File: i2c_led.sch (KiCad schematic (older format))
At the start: 20 parts

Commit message: Worked on BOM.
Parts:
- gave numbers to parts that had none: 20
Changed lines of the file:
@@
 $EndDescr
 $Comp
-L ME2188:ME2188A50XG U?
+L ME2188:ME2188A50XG U2
 U 1 1 6174A4C9
 P 2750 1500
-F 0 "U?" H 2750 1915 50  0000 C CNN
+F 0 "U2" H 2750 1915 50  0000 C CNN
 F 1 "ME2188A50XG" H 2750 1824 50  0000 C CNN
 F 2 "" H 2750 2000 50  0001 C CNN
@@
 $EndComp
 $Comp
-L pspice:INDUCTOR L?
+L pspice:INDUCTOR L1
 U 1 1 6174AC13
 P 1950 1400
-F 0 "L?" H 1950 1615 50  0000 C CNN
+F 0 "L1" H 1950 1615 50  0000 C CNN
 F 1 "22uH" H 1950 1524 50  0000 C CNN
 F 2 "" H 1950 1400 50  0001 C CNN
@@
 	2200 1400 2350 1400
 $Comp
-L power:GND #PWR?
+L power:GND #PWR05
 U 1 1 6174B335
 P 2750 2000
-F 0 "#PWR?" H 2750 1750 50  0001 C CNN
+F 0 "#PWR05" H 2750 1750 50  0001 C CNN
 F 1 "GND" H 2755 1827 50  0000 C CNN
 F 2 "" H 2750 2000 50  0001 C CNN
@@
 $EndComp
 $Comp
-L Device:C C?
+L Device:C C1
 U 1 1 6174BB29
 P 1475 1725
-F 0 "C?" H 1590 1771 50  0000 L CNN
+F 0 "C1" H 1590 1771 50  0000 L CNN
 F 1 "10uF" H 1590 1680 50  0000 L CNN
 F 2 "" H 1513 1575 50  0001 C CNN
@@
 	1475 2000 1475 1875
 $Comp
-L power:GND #PWR?
+L power:GND #PWR01
 U 1 1 6174C089
 P 1475 2000
-F 0 "#PWR?" H 1475 1750 50  0001 C CNN
+F 0 "#PWR01" H 1475 1750 50  0001 C CNN
 F 1 "GND" H 1480 1827 50  0000 C CNN
 F 2 "" H 1475 2000 50  0001 C CNN
@@
 VIN
 $Comp
-L Device:C C?
+L Device:C C4
 U 1 1 6174D112
 P 3475 1725
-F 0 "C?" H 3590 1771 50  0000 L CNN
+F 0 "C4" H 3590 1771 50  0000 L CNN
 F 1 "100uF" H 3590 1680 50  0000 L CNN
 F 2 "" H 3513 1575 50  0001 C CNN
@@
 	3475 2000 3475 1875
 $Comp
-L power:GND #PWR?
+L power:GND #PWR06
 U 1 1 6174E073
 P 3475 2000
-F 0 "#PWR?" H 3475 1750 50  0001 C CNN
+F 0 "#PWR06" H 3475 1750 50  0001 C CNN
 F 1 "GND" H 3480 1827 50  0000 C CNN
 F 2 "" H 3475 2000 50  0001 C CNN
@@
 \nDC-DC converter input 1.8-5V, output 5V\nLCSC Part# C236769
 $Comp
-L Connector_Generic:Conn_01x04 J?
+L Connector_Generic:Conn_01x04 J1
 U 1 1 617588B6
 P 8450 1425
-F 0 "J?" H 8530 1417 50  0000 L CNN
+F 0 "J1" H 8530 1417 50  0000 L CNN
 F 1 "Conn_01x04" H 8530 1326 50  0000 L CNN
 F 2 "" H 8450 1425 50  0001 C CNN
@@
 $EndComp
 $Comp
-L Connector_Generic:Conn_01x04 J?
+L Connector_Generic:Conn_01x04 J2
 U 1 1 617591D1
 P 10050 1425
-F 0 "J?" H 10130 1417 50  0000 L CNN
+F 0 "J2" H 10130 1417 50  0000 L CNN
 F 1 "Conn_01x04" H 10130 1326 50  0000 L CNN
 F 2 "" H 10050 1425 50  0001 C CNN
@@
 SCL_VIN
 $Comp
-L Potentiometer_Digital:MCP4018-xxxxLT U?
+L Potentiometer_Digital:MCP4018-xxxxLT U1
 U 1 1 6175D2CA
 P 1850 4575
-F 0 "U?" H 1850 5050 50  0000 C CNN
+F 0 "U1" H 1850 5050 50  0000 C CNN
 F 1 "MCP4018-xxxxLT" H 2125 4950 50  0000 C CNN
 F 2 "Package_TO_SOT_SMD:SOT-363_SC-70-6" H 1900 4325 50  0001 L CNN
@@
 	1850 5000 1850 4875
 $Comp
-L power:GND #PWR?
+L power:GND #PWR02
 U 1 1 6175F273
 P 1850 5000
-F 0 "#PWR?" H 1850 4750 50  0001 C CNN
+F 0 "#PWR02" H 1850 4750 50  0001 C CNN
 F 1 "GND" H 1855 4827 50  0000 C CNN
 F 2 "" H 1850 5000 50  0001 C CNN
@@
 Stemma QT / qwiic  connectors\nLCSC#  C145956
 $Comp
-L Transistor_FET:BSS138 Q?
+L Transistor_FET:BSS138 Q3
 U 1 1 61765AC4
 P 9100 5000
-F 0 "Q?" V 9349 5000 50  0000 C CNN
+F 0 "Q3" V 9349 5000 50  0000 C CNN
 F 1 "BSS138" V 9440 5000 50  0000 C CNN
 F 2 "Package_TO_SOT_SMD:SOT-23" H 9300 4925 50  0001 L CIN
@@
 $EndComp
 $Comp
-L Transistor_FET:BSS138 Q?
+L Transistor_FET:BSS138 Q2
 U 1 1 61767FC9
 P 8600 4400
-F 0 "Q?" V 8849 4400 50  0000 C CNN
+F 0 "Q2" V 8849 4400 50  0000 C CNN
 F 1 "BSS138" V 8940 4400 50  0000 C CNN
 F 2 "Package_TO_SOT_SMD:SOT-23" H 8800 4325 50  0001 L CIN
@@
 i2c level shifters\nBSS138 LCSC# C78284
 $Comp
-L Device:R R?
+L Device:R R4
 U 1 1 61771F4B
 P 8000 4175
-F 0 "R?" H 8070 4221 50  0000 L CNN
+F 0 "R4" H 8070 4221 50  0000 L CNN
 F 1 "10k" H 8070 4130 50  0000 L CNN
 F 2 "" V 7930 4175 50  0001 C CNN
@@
 $EndComp
 $Comp
-L Device:R R?
+L Device:R R3
 U 1 1 61772E16
 P 7675 4175
-F 0 "R?" H 7745 4221 50  0000 L CNN
+F 0 "R3" H 7745 4221 50  0000 L CNN
 F 1 "10k" H 7745 4130 50  0000 L CNN
 F 2 "" V 7605 4175 50  0001 C CNN
@@
 $EndComp
 $Comp
-L Device:R R?
+L Device:R R6
 U 1 1 61773986
 P 9900 4175
-F 0 "R?" H 9970 4221 50  0000 L CNN
+F 0 "R6" H 9970 4221 50  0000 L CNN
 F 1 "10k" H 9970 4130 50  0000 L CNN
 F 2 "" V 9830 4175 50  0001 C CNN
@@
 $EndComp
 $Comp
-L Device:R R?
+L Device:R R5
 U 1 1 61773B5E
 P 9575 4175
-F 0 "R?" H 9645 4221 50  0000 L CNN
+F 0 "R5" H 9645 4221 50  0000 L CNN
 F 1 "10k" H 9645 4130 50  0000 L CNN
 F 2 "" V 9505 4175 50  0001 C CNN
@@
 MCP4018T-503E/LT\nLCSC# C145561
 $Comp
-L Amplifier_Operational:LMV321 U?
+L Amplifier_Operational:LMV321 U3
 U 1 1 617B3880
 P 3675 4575
-F 0 "U?" H 4019 4621 50  0000 L CNN
+F 0 "U3" H 4019 4621 50  0000 L CNN
 F 1 "LMV321" H 4019 4530 50  0000 L CNN
 F 2 "" H 3675 4575 50  0001 L CNN
@@
 $EndComp
 $Comp
-L Device:R R?
+L Device:R R1
 U 1 1 617B515A
 P 2650 4375
-F 0 "R?" V 2443 4375 50  0000 C CNN
+F 0 "R1" V 2443 4375 50  0000 C CNN
 F 1 "45.3k" V 2534 4375 50  0000 C CNN
 F 2 "" V 2580 4375 50  0001 C CNN
@@
 45.3k  1% 0603 resistor C23058\n24.9    1% 0603  resistor C403105
 $Comp
-L Device:LED_ALT D?
+L Device:LED_ALT D1
 U 1 1 617C0FF2
 P 4875 4050
-F 0 "D?" V 4914 3932 50  0000 R CNN
+F 0 "D1" V 4914 3932 50  0000 R CNN
 F 1 "LED_ALT" V 4823 3932 50  0000 R CNN
 F 2 "" H 4875 4050 50  0001 C CNN
@@
 $EndComp
 $Comp
-L Device:Q_NPN_BEC Q?
+L Device:Q_NPN_BEC Q1
 U 1 1 617C2C7F
 P 4775 4575
-F 0 "Q?" H 4966 4621 50  0000 L CNN
+F 0 "Q1" H 4966 4621 50  0000 L CNN
 F 1 "Q_NPN_BEC" H 4966 4530 50  0000 L CNN
 F 2 "" H 4975 4675 50  0001 C CNN
@@
 	3975 4575 4575 4575
 $Comp
-L Device:R R?
+L Device:R R2
 U 1 1 617C7054
 P 4875 5125
-F 0 "R?" H 4945 5171 50  0000 L CNN
+F 0 "R2" H 4945 5171 50  0000 L CNN
 F 1 "24.9" H 4945 5080 50  0000 L CNN
 F 2 "" V 4805 5125 50  0001 C CNN
@@
 $EndComp
 $Comp
-L power:GND #PWR?
+L power:GND #PWR07
 U 1 1 617BDEF2
 P 3575 5000
-F 0 "#PWR?" H 3575 4750 50  0001 C CNN
+F 0 "#PWR07" H 3575 4750 50  0001 C CNN
 F 1 "GND" H 3580 4827 50  0000 C CNN
 F 2 "" H 3575 5000 50  0001 C CNN
@@
 	3575 5000 3575 4875
 $Comp
-L power:GND #PWR?
+L power:GND #PWR08
 U 1 1 617C9AE1
 P 4875 5400
-F 0 "#PWR?" H 4875 5150 50  0001 C CNN
+F 0 "#PWR08" H 4875 5150 50  0001 C CNN
 F 1 "GND" H 4880 5227 50  0000 C CNN
 F 2 "" H 4875 5400 50  0001 C CNN
@@
 Sikor S8050\nC444723
 $Comp
-L Device:C C?
+L Device:C C2
 U 1 1 617EFAB2
 P 1875 5900
-F 0 "C?" H 1990 5946 50  0000 L CNN
+F 0 "C2" H 1990 5946 50  0000 L CNN
 F 1 "0.1uF" H 1990 5855 50  0000 L CNN
 F 2 "" H 1913 5750 50  0001 C CNN
@@
 $EndComp
 $Comp
-L Device:C C?
+L Device:C C3
 U 1 1 617F0FE6
 P 2650 5900
-F 0 "C?" H 2765 5946 50  0000 L CNN
+F 0 "C3" H 2765 5946 50  0000 L CNN
 F 1 "0.1uF" H 2765 5855 50  0000 L CNN
 F 2 "" H 2688 5750 50  0001 C CNN
@@
 	1875 6175 1875 6050
 $Comp
-L power:GND #PWR?
+L power:GND #PWR03
 U 1 1 617FDA2D
 P 1875 6175
-F 0 "#PWR?" H 1875 5925 50  0001 C CNN
+F 0 "#PWR03" H 1875 5925 50  0001 C CNN
 F 1 "GND" H 1880 6002 50  0000 C CNN
 F 2 "" H 1875 6175 50  0001 C CNN
@@
 	2650 6175 2650 6050
 $Comp
-L power:GND #PWR?
+L power:GND #PWR04
 U 1 1 618001D5
 P 2650 6175
-F 0 "#PWR?" H 2650 5925 50  0001 C CNN
+F 0 "#PWR04" H 2650 5925 50  0001 C CNN
 F 1 "GND" H 2655 6002 50  0000 C CNN
 F 2 "" H 2650 6175 50  0001 C CNN

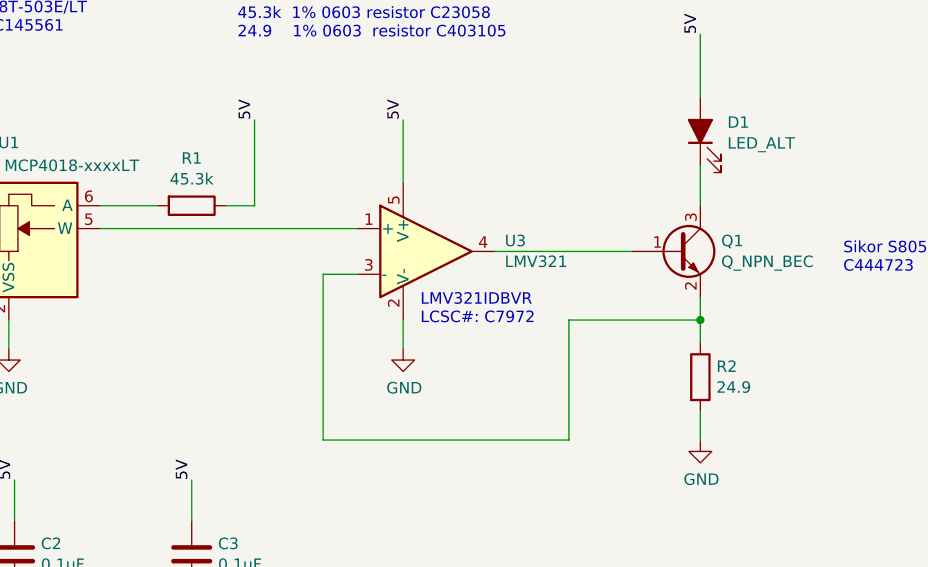
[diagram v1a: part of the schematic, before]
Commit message: Work on BOM and footprint assignments.
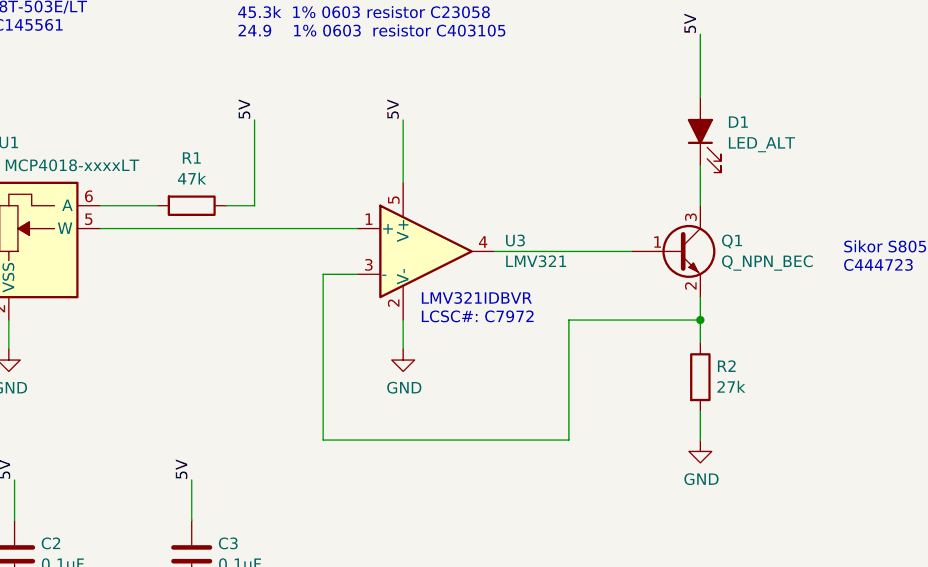
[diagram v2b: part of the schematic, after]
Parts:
- C1, C2, C3: footprint (none) -> Capacitor_SMD:C_0603_1608Metric
- C4: footprint (none) -> Capacitor_SMD:C_0805_2012Metric
- D1: footprint (none) -> LED_SMD:LED_0603_1608Metric
- L1: footprint (none) -> Inductor_SMD:L_1206_3216Metric
- R1: value 45.3k -> 47k
- R2: value 24.9 -> 27k
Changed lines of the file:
@@
 F 0 "L1" H 1950 1615 50  0000 C CNN
 F 1 "22uH" H 1950 1524 50  0000 C CNN
-F 2 "" H 1950 1400 50  0001 C CNN
+F 2 "Inductor_SMD:L_1206_3216Metric" H 1950 1400 50  0001 C CNN
 F 3 "~" H 1950 1400 50  0001 C CNN
 	1    1950 1400
@@
 F 0 "C1" H 1590 1771 50  0000 L CNN
 F 1 "10uF" H 1590 1680 50  0000 L CNN
-F 2 "" H 1513 1575 50  0001 C CNN
+F 2 "Capacitor_SMD:C_0603_1608Metric" H 1513 1575 50  0001 C CNN
 F 3 "~" H 1475 1725 50  0001 C CNN
 	1    1475 1725
@@
 F 0 "C4" H 3590 1771 50  0000 L CNN
 F 1 "100uF" H 3590 1680 50  0000 L CNN
-F 2 "" H 3513 1575 50  0001 C CNN
+F 2 "Capacitor_SMD:C_0805_2012Metric" H 3513 1575 50  0001 C CNN
 F 3 "~" H 3475 1725 50  0001 C CNN
 	1    3475 1725
@@
 P 2650 4375
 F 0 "R1" V 2443 4375 50  0000 C CNN
-F 1 "45.3k" V 2534 4375 50  0000 C CNN
+F 1 "47k" V 2534 4375 50  0000 C CNN
 F 2 "" V 2580 4375 50  0001 C CNN
 F 3 "~" H 2650 4375 50  0001 C CNN
@@
 F 0 "D1" V 4914 3932 50  0000 R CNN
 F 1 "LED_ALT" V 4823 3932 50  0000 R CNN
-F 2 "" H 4875 4050 50  0001 C CNN
+F 2 "LED_SMD:LED_0603_1608Metric" H 4875 4050 50  0001 C CNN
 F 3 "~" H 4875 4050 50  0001 C CNN
 	1    4875 4050
@@
 P 4875 5125
 F 0 "R2" H 4945 5171 50  0000 L CNN
-F 1 "24.9" H 4945 5080 50  0000 L CNN
+F 1 "27k" H 4945 5080 50  0000 L CNN
 F 2 "" V 4805 5125 50  0001 C CNN
 F 3 "~" H 4875 5125 50  0001 C CNN
@@
 F 0 "C2" H 1990 5946 50  0000 L CNN
 F 1 "0.1uF" H 1990 5855 50  0000 L CNN
-F 2 "" H 1913 5750 50  0001 C CNN
+F 2 "Capacitor_SMD:C_0603_1608Metric" H 1913 5750 50  0001 C CNN
 F 3 "~" H 1875 5900 50  0001 C CNN
 	1    1875 5900
@@
 F 0 "C3" H 2765 5946 50  0000 L CNN
 F 1 "0.1uF" H 2765 5855 50  0000 L CNN
-F 2 "" H 2688 5750 50  0001 C CNN
+F 2 "Capacitor_SMD:C_0603_1608Metric" H 2688 5750 50  0001 C CNN
 F 3 "~" H 2650 5900 50  0001 C CNN
 	1    2650 5900

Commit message: Worked on layout.
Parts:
- J1, J2: footprint (none) -> BOOMELE_SH_SMD:BOOMELE_SMD_SH_4PIN_RT
- Q1, U2: footprint (none) -> Package_TO_SOT_SMD:SOT-23
- R1, R2, R3, R4, R5, R6: footprint (none) -> Resistor_SMD:R_0603_1608Metric
- U3: footprint (none) -> Package_TO_SOT_SMD:SOT-23-5
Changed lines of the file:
@@
 F 0 "U2" H 2750 1915 50  0000 C CNN
 F 1 "ME2188A50XG" H 2750 1824 50  0000 C CNN
-F 2 "" H 2750 2000 50  0001 C CNN
+F 2 "Package_TO_SOT_SMD:SOT-23" H 2750 2000 50  0001 C CNN
 F 3 "" H 2750 2000 50  0001 C CNN
 	1    2750 1500
@@
 F 0 "J1" H 8530 1417 50  0000 L CNN
 F 1 "Conn_01x04" H 8530 1326 50  0000 L CNN
-F 2 "" H 8450 1425 50  0001 C CNN
+F 2 "BOOMELE_SH_SMD:BOOMELE_SMD_SH_4PIN_RT" H 8450 1425 50  0001 C CNN
 F 3 "~" H 8450 1425 50  0001 C CNN
 	1    8450 1425
@@
 F 0 "J2" H 10130 1417 50  0000 L CNN
 F 1 "Conn_01x04" H 10130 1326 50  0000 L CNN
-F 2 "" H 10050 1425 50  0001 C CNN
+F 2 "BOOMELE_SH_SMD:BOOMELE_SMD_SH_4PIN_RT" H 10050 1425 50  0001 C CNN
 F 3 "~" H 10050 1425 50  0001 C CNN
 	1    10050 1425
@@
 F 0 "R4" H 8070 4221 50  0000 L CNN
 F 1 "10k" H 8070 4130 50  0000 L CNN
-F 2 "" V 7930 4175 50  0001 C CNN
+F 2 "Resistor_SMD:R_0603_1608Metric" V 7930 4175 50  0001 C CNN
 F 3 "~" H 8000 4175 50  0001 C CNN
 	1    8000 4175
@@
 F 0 "R3" H 7745 4221 50  0000 L CNN
 F 1 "10k" H 7745 4130 50  0000 L CNN
-F 2 "" V 7605 4175 50  0001 C CNN
+F 2 "Resistor_SMD:R_0603_1608Metric" V 7605 4175 50  0001 C CNN
 F 3 "~" H 7675 4175 50  0001 C CNN
 	1    7675 4175
@@
 F 0 "R6" H 9970 4221 50  0000 L CNN
 F 1 "10k" H 9970 4130 50  0000 L CNN
-F 2 "" V 9830 4175 50  0001 C CNN
+F 2 "Resistor_SMD:R_0603_1608Metric" V 9830 4175 50  0001 C CNN
 F 3 "~" H 9900 4175 50  0001 C CNN
 	1    9900 4175
@@
 F 0 "R5" H 9645 4221 50  0000 L CNN
 F 1 "10k" H 9645 4130 50  0000 L CNN
-F 2 "" V 9505 4175 50  0001 C CNN
+F 2 "Resistor_SMD:R_0603_1608Metric" V 9505 4175 50  0001 C CNN
 F 3 "~" H 9575 4175 50  0001 C CNN
 	1    9575 4175
@@
 F 0 "U3" H 4019 4621 50  0000 L CNN
 F 1 "LMV321" H 4019 4530 50  0000 L CNN
-F 2 "" H 3675 4575 50  0001 L CNN
+F 2 "Package_TO_SOT_SMD:SOT-23-5" H 3675 4575 50  0001 L CNN
 F 3 "http://www.ti.com/lit/ds/symlink/lmv324.pdf" H 3675 4575 50  0001 C CNN
 	1    3675 4575
@@
 F 0 "R1" V 2443 4375 50  0000 C CNN
 F 1 "47k" V 2534 4375 50  0000 C CNN
-F 2 "" V 2580 4375 50  0001 C CNN
+F 2 "Resistor_SMD:R_0603_1608Metric" V 2580 4375 50  0001 C CNN
 F 3 "~" H 2650 4375 50  0001 C CNN
 	1    2650 4375
@@
 F 0 "Q1" H 4966 4621 50  0000 L CNN
 F 1 "Q_NPN_BEC" H 4966 4530 50  0000 L CNN
-F 2 "" H 4975 4675 50  0001 C CNN
+F 2 "Package_TO_SOT_SMD:SOT-23" H 4975 4675 50  0001 C CNN
 F 3 "~" H 4775 4575 50  0001 C CNN
 	1    4775 4575
@@
 F 0 "R2" H 4945 5171 50  0000 L CNN
 F 1 "27k" H 4945 5080 50  0000 L CNN
-F 2 "" V 4805 5125 50  0001 C CNN
+F 2 "Resistor_SMD:R_0603_1608Metric" V 4805 5125 50  0001 C CNN
 F 3 "~" H 4875 5125 50  0001 C CNN
 	1    4875 5125

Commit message: Worked on layout.
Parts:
- C1, C2, C3: footprint Capacitor_SMD:C_0603_1608Metric -> Capacitor_SMD:C_0402_1005Metric
- R1, R2, R3, R4, R5, R6: footprint Resistor_SMD:R_0603_1608Metric -> Resistor_SMD:R_0402_1005Metric
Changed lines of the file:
@@
 F 0 "C1" H 1590 1771 50  0000 L CNN
 F 1 "10uF" H 1590 1680 50  0000 L CNN
-F 2 "Capacitor_SMD:C_0603_1608Metric" H 1513 1575 50  0001 C CNN
+F 2 "Capacitor_SMD:C_0402_1005Metric" H 1513 1575 50  0001 C CNN
 F 3 "~" H 1475 1725 50  0001 C CNN
 	1    1475 1725
@@
 F 0 "R4" H 8070 4221 50  0000 L CNN
 F 1 "10k" H 8070 4130 50  0000 L CNN
-F 2 "Resistor_SMD:R_0603_1608Metric" V 7930 4175 50  0001 C CNN
+F 2 "Resistor_SMD:R_0402_1005Metric" V 7930 4175 50  0001 C CNN
 F 3 "~" H 8000 4175 50  0001 C CNN
 	1    8000 4175
@@
 F 0 "R3" H 7745 4221 50  0000 L CNN
 F 1 "10k" H 7745 4130 50  0000 L CNN
-F 2 "Resistor_SMD:R_0603_1608Metric" V 7605 4175 50  0001 C CNN
+F 2 "Resistor_SMD:R_0402_1005Metric" V 7605 4175 50  0001 C CNN
 F 3 "~" H 7675 4175 50  0001 C CNN
 	1    7675 4175
@@
 F 0 "R6" H 9970 4221 50  0000 L CNN
 F 1 "10k" H 9970 4130 50  0000 L CNN
-F 2 "Resistor_SMD:R_0603_1608Metric" V 9830 4175 50  0001 C CNN
+F 2 "Resistor_SMD:R_0402_1005Metric" V 9830 4175 50  0001 C CNN
 F 3 "~" H 9900 4175 50  0001 C CNN
 	1    9900 4175
@@
 F 0 "R5" H 9645 4221 50  0000 L CNN
 F 1 "10k" H 9645 4130 50  0000 L CNN
-F 2 "Resistor_SMD:R_0603_1608Metric" V 9505 4175 50  0001 C CNN
+F 2 "Resistor_SMD:R_0402_1005Metric" V 9505 4175 50  0001 C CNN
 F 3 "~" H 9575 4175 50  0001 C CNN
 	1    9575 4175
@@
 F 0 "R1" V 2443 4375 50  0000 C CNN
 F 1 "47k" V 2534 4375 50  0000 C CNN
-F 2 "Resistor_SMD:R_0603_1608Metric" V 2580 4375 50  0001 C CNN
+F 2 "Resistor_SMD:R_0402_1005Metric" V 2580 4375 50  0001 C CNN
 F 3 "~" H 2650 4375 50  0001 C CNN
 	1    2650 4375
@@
 F 0 "R2" H 4945 5171 50  0000 L CNN
 F 1 "27k" H 4945 5080 50  0000 L CNN
-F 2 "Resistor_SMD:R_0603_1608Metric" V 4805 5125 50  0001 C CNN
+F 2 "Resistor_SMD:R_0402_1005Metric" V 4805 5125 50  0001 C CNN
 F 3 "~" H 4875 5125 50  0001 C CNN
 	1    4875 5125
@@
 F 0 "C2" H 1990 5946 50  0000 L CNN
 F 1 "0.1uF" H 1990 5855 50  0000 L CNN
-F 2 "Capacitor_SMD:C_0603_1608Metric" H 1913 5750 50  0001 C CNN
+F 2 "Capacitor_SMD:C_0402_1005Metric" H 1913 5750 50  0001 C CNN
 F 3 "~" H 1875 5900 50  0001 C CNN
 	1    1875 5900
@@
 F 0 "C3" H 2765 5946 50  0000 L CNN
 F 1 "0.1uF" H 2765 5855 50  0000 L CNN
-F 2 "Capacitor_SMD:C_0603_1608Metric" H 2688 5750 50  0001 C CNN
+F 2 "Capacitor_SMD:C_0402_1005Metric" H 2688 5750 50  0001 C CNN
 F 3 "~" H 2650 5900 50  0001 C CNN
 	1    2650 5900

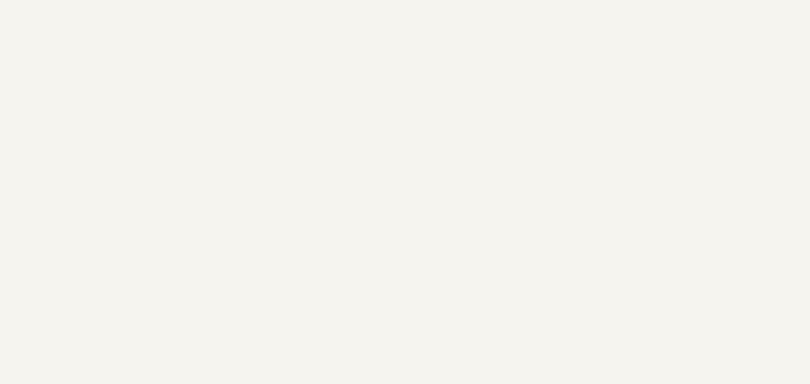
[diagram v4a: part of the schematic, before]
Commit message: Finished initial layout and routing.
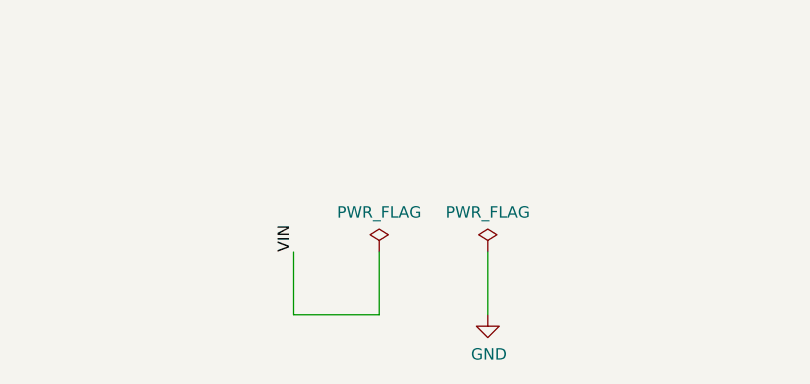
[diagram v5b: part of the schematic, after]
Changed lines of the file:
@@
+	1    0    0    -1
+$EndComp
+$Comp
+L power:PWR_FLAG #FLG0101
+U 1 1 618C7AAE
+P 6625 6825
+F 0 "#FLG0101" H 6625 6900 50  0001 C CNN
+F 1 "PWR_FLAG" H 6625 6998 50  0000 C CNN
+F 2 "" H 6625 6825 50  0001 C CNN
+F 3 "~" H 6625 6825 50  0001 C CNN
+	1    6625 6825
+	1    0    0    -1
+$EndComp
+$Comp
+L power:PWR_FLAG #FLG0102
+U 1 1 618C935B
+P 6150 6825
+F 0 "#FLG0102" H 6150 6900 50  0001 C CNN
+F 1 "PWR_FLAG" H 6150 6998 50  0000 C CNN
+F 2 "" H 6150 6825 50  0001 C CNN
+F 3 "~" H 6150 6825 50  0001 C CNN
+	1    6150 6825
+	1    0    0    -1
+$EndComp
+Wire Wire Line
+	6150 6825 6150 7100
+Wire Wire Line
+	6150 7100 5775 7100
+Wire Wire Line
+	5775 7100 5775 6825
+Text Label 5775 6825 1    50   ~ 0
+VIN
+Wire Wire Line
+	6625 6825 6625 7100
+$Comp
+L power:GND #PWR0101
+U 1 1 618D2424
+P 6625 7100
+F 0 "#PWR0101" H 6625 6850 50  0001 C CNN
+F 1 "GND" H 6630 6927 50  0000 C CNN
+F 2 "" H 6625 7100 50  0001 C CNN
+F 3 "" H 6625 7100 50  0001 C CNN
+	1    6625 7100
 	1    0    0    -1
 $EndComp
